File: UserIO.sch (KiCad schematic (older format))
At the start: 3 parts

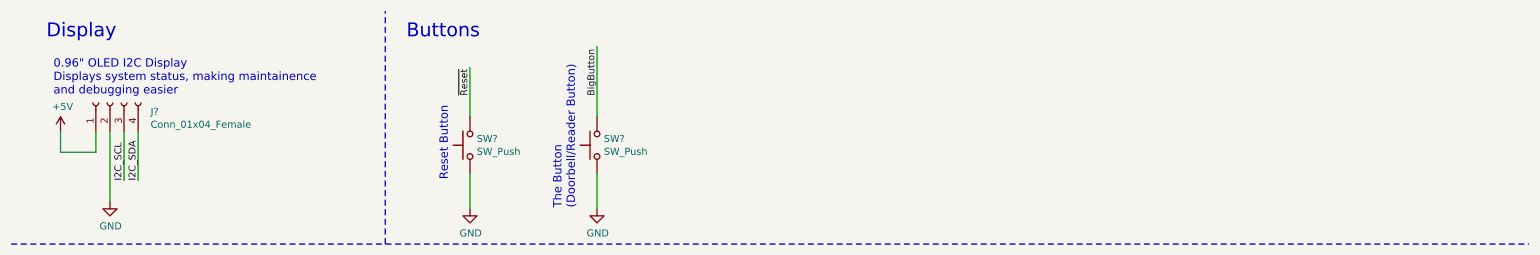
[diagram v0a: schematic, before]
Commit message: Annotated some symbols and linked nets properly between sheets
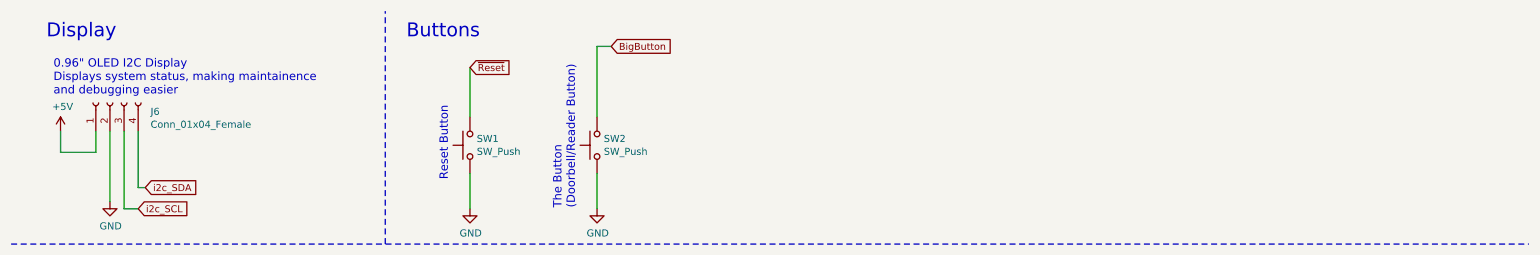
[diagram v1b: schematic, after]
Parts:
- J6: renamed from J?; footprint (none) -> Connector_PinHeader_2.54mm:PinHeader_1x04_P2.54mm_Vertical
- SW1, SW2: renamed from SW?; footprint (none) -> Button_Switch_THT:SW_PUSH_6mm
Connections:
- net labels added: i2c_SCL, i2c_SDA
- net labels removed: I2C_SCL, I2C_SDA
- wire segments 10 -> 13
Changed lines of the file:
@@
 Display
 $Comp
-L Connector:Conn_01x04_Female J?
+L Connector:Conn_01x04_Female J6
 U 1 1 600C1DD9
 P 1150 1150
-F 0 "J?" V 1088 862 50  0000 R CNN
+F 0 "J6" V 1088 862 50  0000 R CNN
 F 1 "Conn_01x04_Female" V 997 862 50  0000 R CNN
-F 2 "" H 1150 1150 50  0001 C CNN
+F 2 "Connector_PinHeader_2.54mm:PinHeader_1x04_P2.54mm_Vertical" H 1150 1150 50  0001 C CNN
 F 3 "~" H 1150 1150 50  0001 C CNN
 	1    1150 1150
@@
 $EndComp
 $Comp
-L power:GND #PWR?
+L power:GND #PWR03
 U 1 1 600C30F8
 P 1150 1850
-F 0 "#PWR?" H 1150 1600 50  0001 C CNN
+F 0 "#PWR03" H 1150 1600 50  0001 C CNN
 F 1 "GND" H 1155 1677 50  0000 C CNN
 F 2 "" H 1150 1850 50  0001 C CNN
@@
 $EndComp
 $Comp
-L power:+5V #PWR?
+L power:+5V #PWR02
 U 1 1 600C3553
 P 800 1350
-F 0 "#PWR?" H 800 1200 50  0001 C CNN
+F 0 "#PWR02" H 800 1200 50  0001 C CNN
 F 1 "+5V" H 815 1523 50  0000 C CNN
 F 2 "" H 800 1350 50  0001 C CNN
@@
 	1    0    0    -1
 $EndComp
-Text Label 1250 1700 1    49   ~ 0
-I2C_SCL
-Text Label 1350 1700 1    49   ~ 0
-I2C_SDA
 Wire Wire Line
 	1150 1350 1150 1850
-Wire Wire Line
-	1250 1700 1250 1350
-Wire Wire Line
-	1350 1350 1350 1700
 Wire Wire Line
 	800  1350 800  1500
@@
 Buttons
 $Comp
-L Switch:SW_Push SW?
+L Switch:SW_Push SW1
 U 1 1 600DF6C9
 P 3700 1450
-F 0 "SW?" V 3746 1402 50  0000 R CNN
+F 0 "SW1" V 3746 1402 50  0000 R CNN
 F 1 "SW_Push" V 3655 1402 50  0000 R CNN
-F 2 "" H 3700 1650 50  0001 C CNN
+F 2 "Button_Switch_THT:SW_PUSH_6mm" H 3700 1650 50  0001 C CNN
 F 3 "~" H 3700 1650 50  0001 C CNN
 	1    3700 1450
@@
 $EndComp
 $Comp
-L power:GND #PWR?
+L power:GND #PWR04
 U 1 1 600E013C
 P 3700 1900
-F 0 "#PWR?" H 3700 1650 50  0001 C CNN
+F 0 "#PWR04" H 3700 1650 50  0001 C CNN
 F 1 "GND" H 3705 1727 50  0000 C CNN
 F 2 "" H 3700 1900 50  0001 C CNN
@@
 Wire Wire Line
 	3700 1900 3700 1650
-Text Label 3700 1100 1    49   ~ 0
-~Reset
 Wire Wire Line
 	3700 1250 3700 900
@@
 Reset Button
 $Comp
-L Switch:SW_Push SW?
+L Switch:SW_Push SW2
 U 1 1 600EC78F
 P 4600 1450
-F 0 "SW?" V 4646 1402 50  0000 R CNN
+F 0 "SW2" V 4646 1402 50  0000 R CNN
 F 1 "SW_Push" V 4555 1402 50  0000 R CNN
-F 2 "" H 4600 1650 50  0001 C CNN
+F 2 "Button_Switch_THT:SW_PUSH_6mm" H 4600 1650 50  0001 C CNN
 F 3 "~" H 4600 1650 50  0001 C CNN
 	1    4600 1450
@@
 $EndComp
 $Comp
-L power:GND #PWR?
+L power:GND #PWR05
 U 1 1 600EEBA2
 P 4600 1900
-F 0 "#PWR?" H 4600 1650 50  0001 C CNN
+F 0 "#PWR05" H 4600 1650 50  0001 C CNN
 F 1 "GND" H 4605 1727 50  0000 C CNN
 F 2 "" H 4600 1900 50  0001 C CNN
@@
 Wire Wire Line
 	4600 1900 4600 1650
-Text Label 4600 1100 1    49   ~ 0
-BigButton
 Wire Wire Line
 	4600 1250 4600 750
 Text Notes 4450 1900 1    59   ~ 0
 The Button\n(Doorbell/Reader Button)
+Text GLabel 1350 1900 2    49   Input ~ 0
+i2c_SCL
+Text GLabel 1400 1750 2    49   Input ~ 0
+i2c_SDA
+Wire Wire Line
+	1350 1750 1400 1750
+Wire Wire Line
+	1350 1350 1350 1750
+Wire Wire Line
+	1250 1900 1350 1900
+Wire Wire Line
+	1250 1350 1250 1900
+Text GLabel 3700 900  2    49   Input ~ 0
+~Reset
+Text GLabel 4700 750  2    49   Input ~ 0
+BigButton
+Wire Wire Line
+	4700 750  4600 750
 $EndSCHEMATC
